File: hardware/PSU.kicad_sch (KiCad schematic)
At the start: 11 parts, among them U2 MAX77751FEFG+

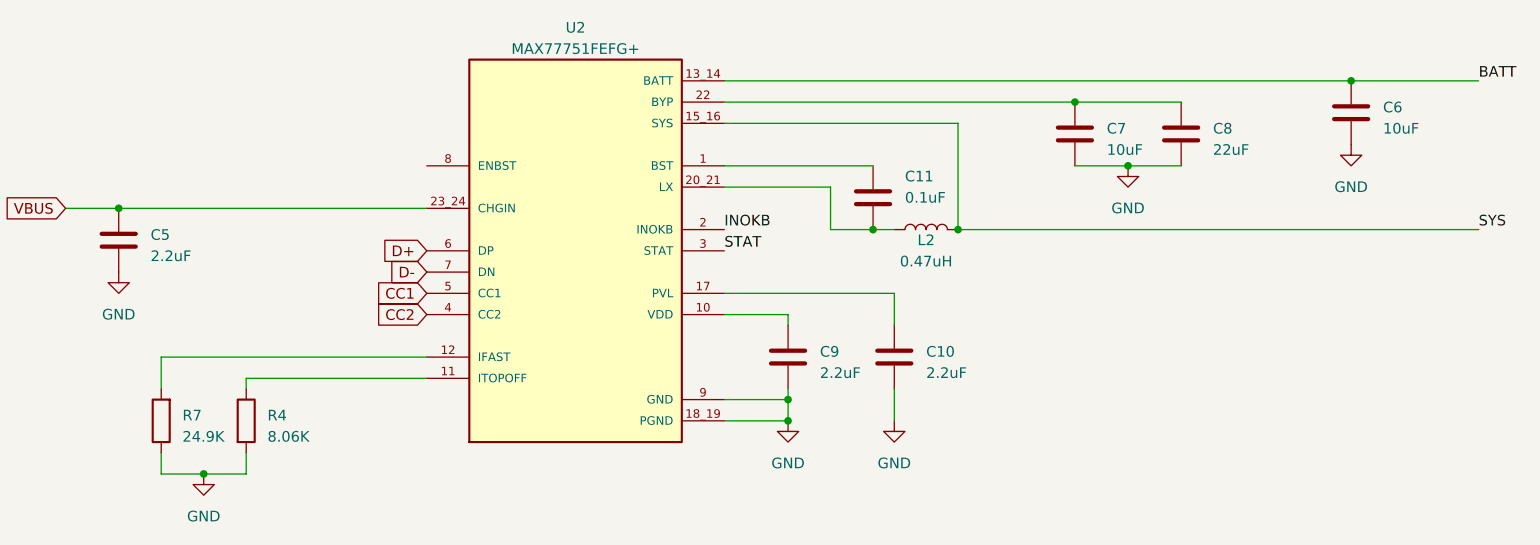
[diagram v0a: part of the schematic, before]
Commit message: finished cahrging curcuit
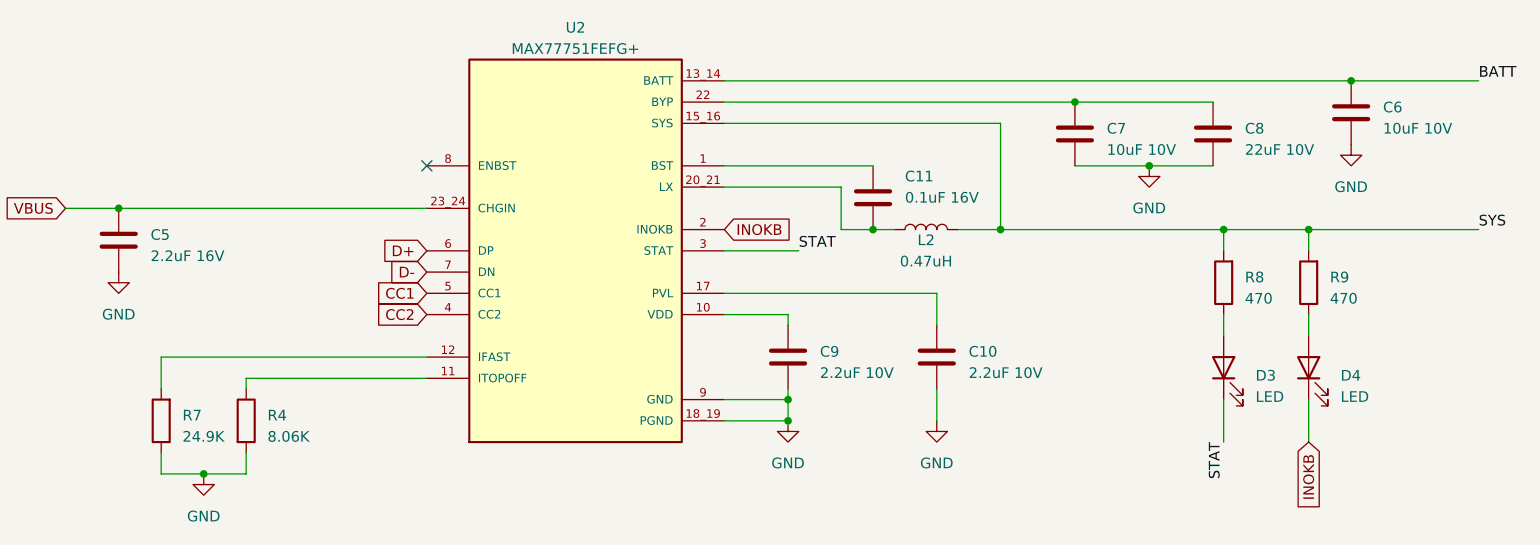
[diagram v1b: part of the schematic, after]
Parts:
- added D3, D4: LED, symbol Device:LED
- added R8, R9: 470, Resistor_SMD:R_0603_1608Metric_Pad0.98x0.95mm_HandSolder, symbol Device:R
- C10, C9: value 2.2uF -> 2.2uF 10V
- C11: value 0.1uF -> 0.1uF 16V
- C5: value 2.2uF -> 2.2uF 16V
- C6, C7: value 10uF -> 10uF 10V
- C8: value 22uF -> 22uF 10V
- L2: footprint (none) -> CIGT201610EHR47MNE:INDC2016X80N
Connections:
- net INOKB: now also D4.1 (K)
- net STAT: now also D3.1 (K)
- net SYS: now also R8.2, R9.2
- new net: D4.2 (A), R9.1
- new net: D3.2 (A), R8.1
- no-connect marks 0 -> 1
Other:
- moved on the sheet: C10, C8

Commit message: added 3v3 ldo
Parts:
- added C12, C13: 10uF 10V, Capacitor_SMD:C_0603_1608Metric, symbol Device:C
- added IC1: TPS74533PCQWDRVRQ1, TPS74533PCQWDRVRQ1:SON65P200X200X80-7N, symbol TPS74533PCQWDRVRQ1:TPS74533PCQWDRVRQ1
- added J7: Conn_01x02_Pin, symbol Connector:Conn_01x02_Pin
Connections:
- net BATT: now also J7.1 (Pin_1)
- net GND: now also C12.2, C13.2, IC1.3 (GND), IC1.7 (EP), J7.2 (Pin_2)
- net SYS: now also C13.1, IC1.4 (EN), IC1.6 (IN)
- new net 3V3: C12.1, IC1.1 (OUT)
- no-connect marks 1 -> 2

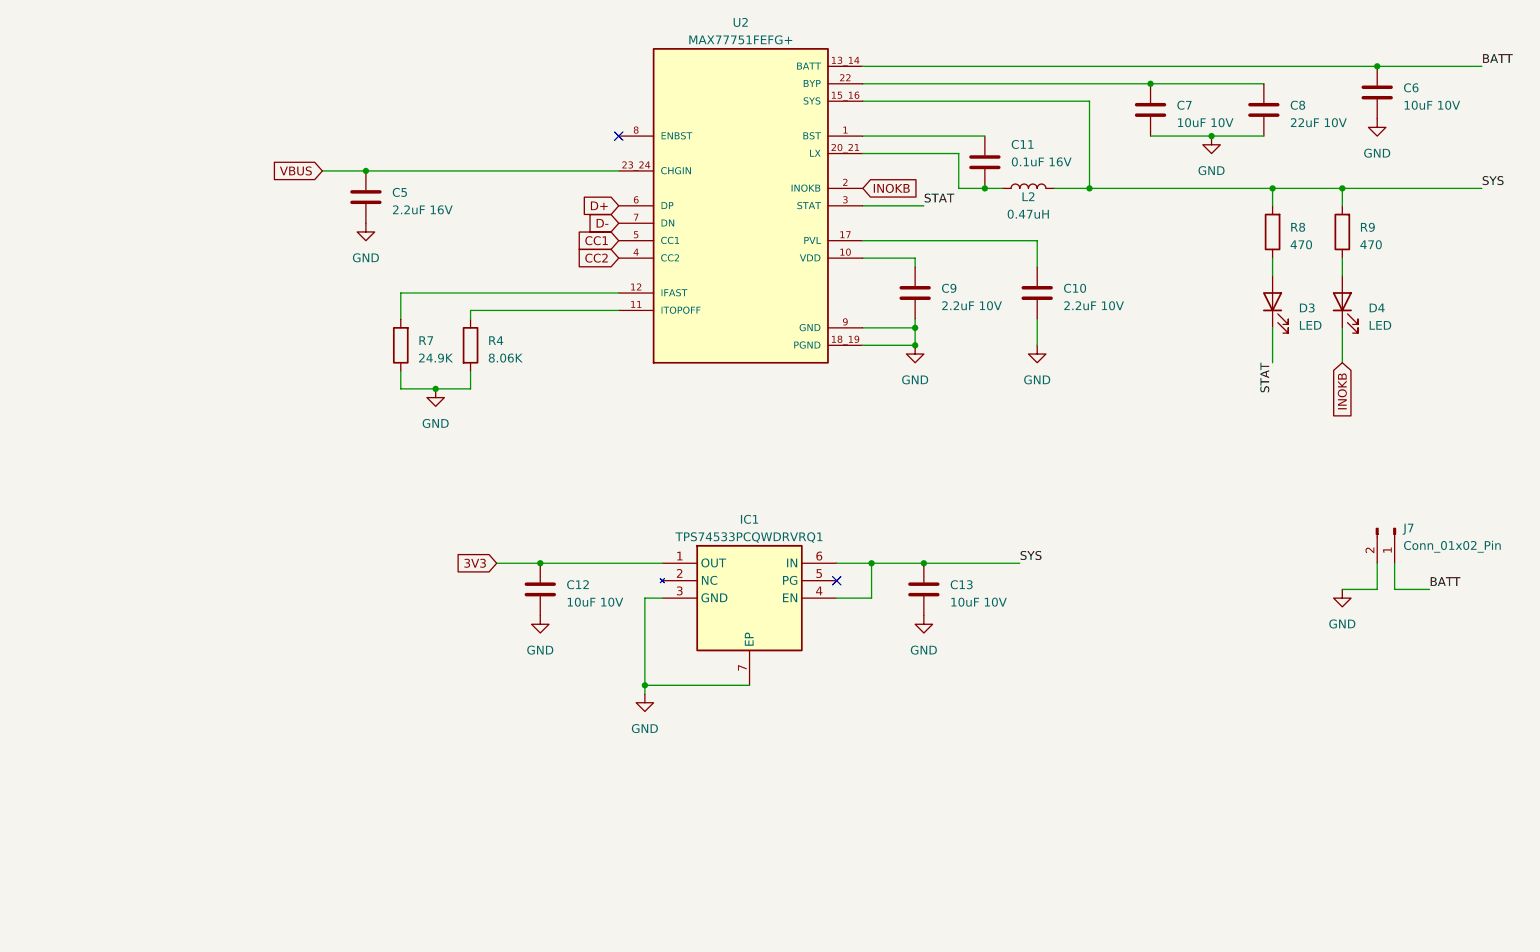
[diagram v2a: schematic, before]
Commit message: added power latching circuit
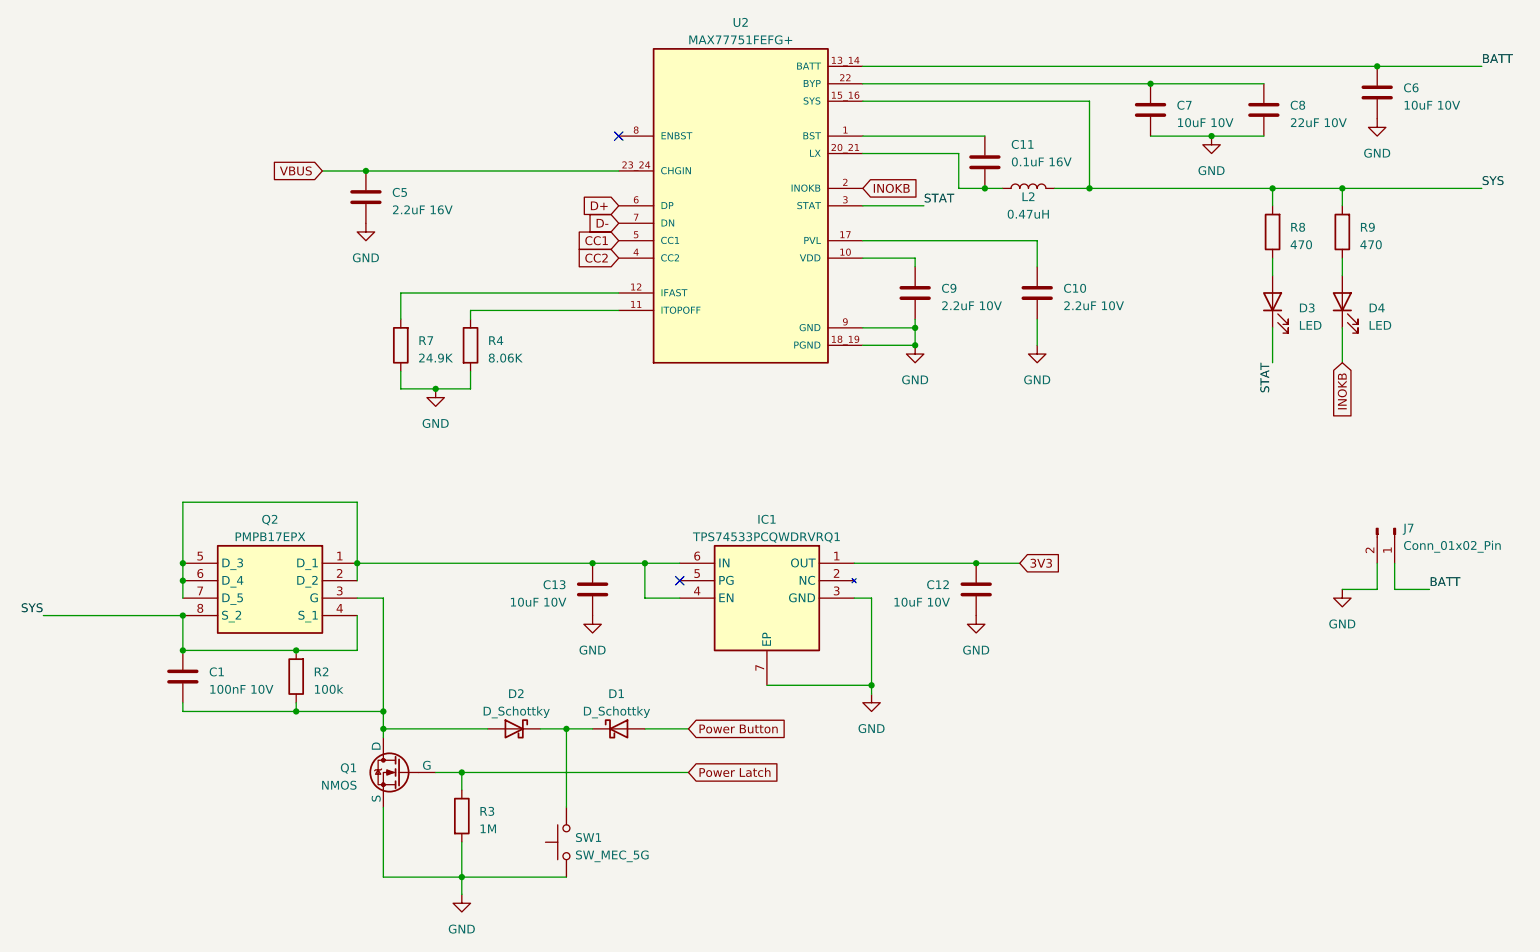
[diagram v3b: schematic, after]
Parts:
- added C1: 100nF 10V, Capacitor_SMD:C_0603_1608Metric, symbol Device:C
- added D1, D2: D_Schottky, symbol Device:D_Schottky
- added Q1: NMOS, symbol Simulation_SPICE:NMOS
- added Q2: PMPB17EPX, PMPB17EPX:PMPB17EPX, symbol PMPB17EPX:PMPB17EPX
- added R2: 100k, Resistor_SMD:R_0603_1608Metric_Pad0.98x0.95mm_HandSolder, symbol Device:R
- added R3: 1M, Resistor_SMD:R_0402_1005Metric, symbol Device:R
- added SW1: SW_MEC_5G, symbol Switch:SW_MEC_5G
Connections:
- net GND: now also Q1.3 (S), R3.2, SW1.1 (A), SW1.2 (A)
- net SYS: now also C1.1, Q2.4 (S_1), Q2.8 (S_2), R2.2; no longer C13.1, IC1.4 (EN), IC1.6 (IN)
- new net: D1.1 (K), D2.1 (K), SW1.3 (B), SW1.4 (B)
- new net: C1.2, D2.2 (A), Q1.1 (D), Q2.3 (G), R2.1
- new net: C13.1, IC1.4 (EN), IC1.6 (IN), Q2.1 (D_1), Q2.2 (D_2), Q2.5 (D_3), Q2.6 (D_4), Q2.7 (D_5)
- new net Power Button: D1.2 (A)
- new net Power Latch: Q1.2 (G), R3.1
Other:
- moved on the sheet: C12, C13, IC1
